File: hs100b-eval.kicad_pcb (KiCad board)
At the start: 2 copper layers, 60 x 50 mm, 42 parts, among them IC1 HS-100B, J1 USB_B_Micro, J2 SPKR, J20 RADIO_DATA, J3 MIC, SW1 MUTE_REC, SW2 MUTE_PLAY, SW3 VOL_DN, SW4 VOL_UP, SW5 SW_DIP_x03

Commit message: Swap Diptronics switches for smaller Wurth one
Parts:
- SW5: footprint Diptronics:DMR -> Wurth:416131160803
- moved TP3 18.2 mm to (135.5, 72.0)
- moved C9 7.91 mm to (184.0, 95.0)
- moved SW5 1.06 mm to (139.5, 77.0)
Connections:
- net Net-(C3-Pad1) renamed /AVDD1
- net Net-(C5-Pad1) renamed /AVDD2
- net Net-(IC1-Pad35) renamed /DVDD
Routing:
- net Net-(C9-Pad2): track 14.3 -> 19.5 mm
- net /MODE: track 28.9 -> 31.6 mm
- net /PWRSEL: track 24.6 -> 26.2 mm
- net +3V3: track 38.1 -> 37.4 mm
- net /MSEL: track 30.7 -> 31.0 mm, vias 3 -> 2
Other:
- board text added: "HS100B Audio Evaluation Board v4 C. Keller 2021-04-21 https://github.com/k0swe/hs100b-eval"
- board text removed: "HS100B Audio Evaluation Board v3 C. Keller 2021-04-21 https://github.com/k0swe/hs100b-eval"

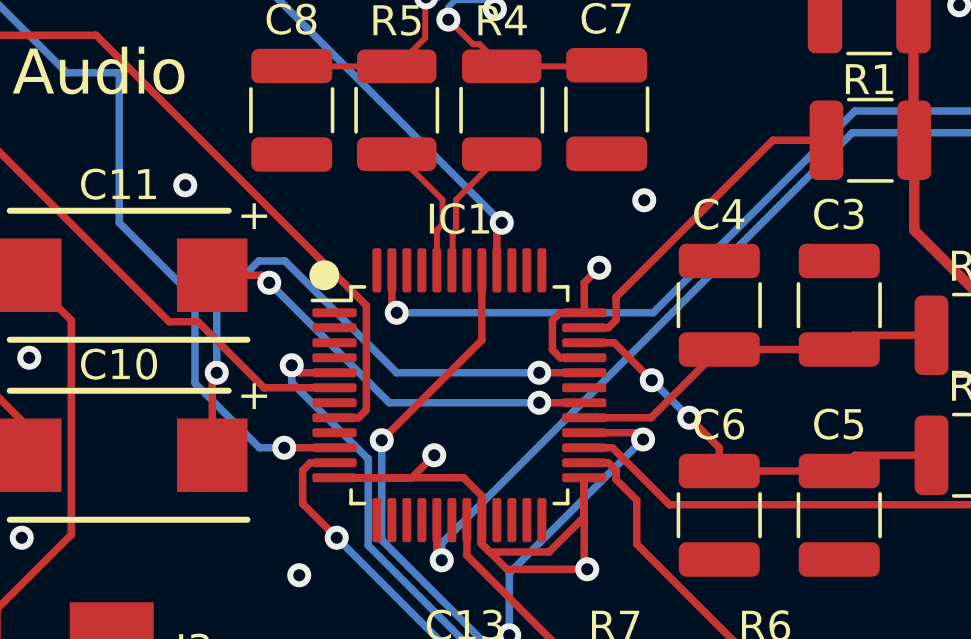
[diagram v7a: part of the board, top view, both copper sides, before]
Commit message: Fix R and L channels
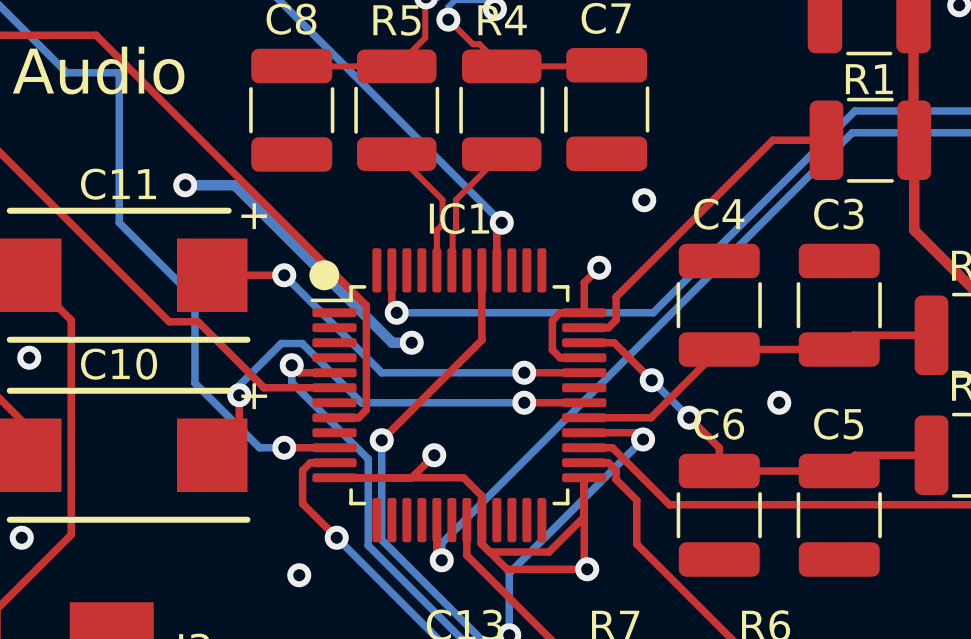
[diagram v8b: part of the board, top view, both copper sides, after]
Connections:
- IC1 pad 30: Net-(C11-Pad1) -> Net-(C10-Pad1)
- IC1 pad 32: Net-(C10-Pad1) -> Net-(C11-Pad1)
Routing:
- net GND: track 40.7 -> 50.4 mm, vias 18 -> 20
- net Net-(C10-Pad1): track 19.5 -> 15.6 mm
